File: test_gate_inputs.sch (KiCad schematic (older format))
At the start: 24 parts

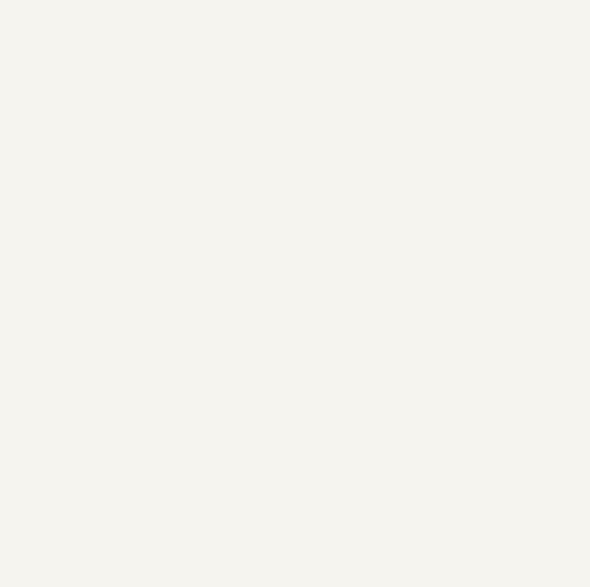
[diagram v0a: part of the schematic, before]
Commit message: add pin header connector
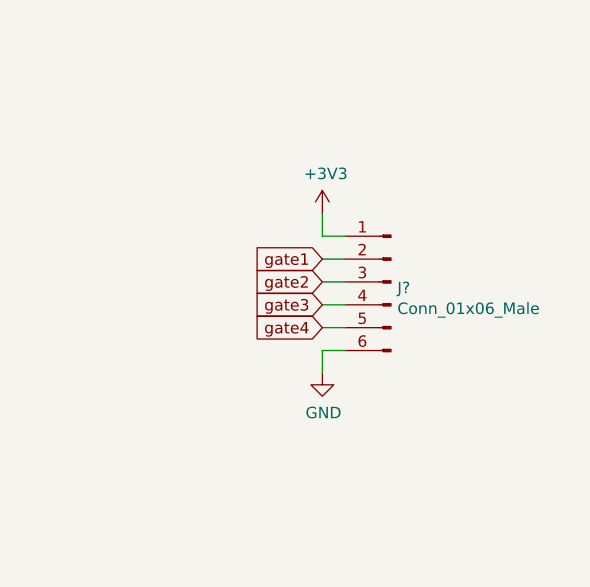
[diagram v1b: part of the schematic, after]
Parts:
- added J?: Conn_01x06_Male, symbol Connector:Conn_01x06_Male
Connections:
- net +3V3: now also J?.1 (Pin_1)
- net GND: now also J?.6 (Pin_6)
- new net gate1: J?.2 (Pin_2)
- new net gate2: J?.3 (Pin_3)
- new net gate3: J?.4 (Pin_4)
- new net gate4: J?.5 (Pin_5)
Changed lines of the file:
@@
 Wire Wire Line
 	3300 6500 3300 6700
+$Comp
+L Connector:Conn_01x06_Male J?
+U 1 1 6128B18E
+P 6500 3350
+F 0 "J?" H 6472 3324 50  0000 R CNN
+F 1 "Conn_01x06_Male" H 6472 3233 50  0000 R CNN
+F 2 "" H 6500 3350 50  0001 C CNN
+F 3 "~" H 6500 3350 50  0001 C CNN
+	1    6500 3350
+	-1   0    0    -1
+$EndComp
+$Comp
+L power:+3V3 #PWR?
+U 1 1 61293AED
+P 6200 3050
+F 0 "#PWR?" H 6200 2900 50  0001 C CNN
+F 1 "+3V3" H 6215 3223 50  0000 C CNN
+F 2 "" H 6200 3050 50  0001 C CNN
+F 3 "" H 6200 3050 50  0001 C CNN
+	1    6200 3050
+	1    0    0    -1
+$EndComp
+$Comp
+L power:GND #PWR?
+U 1 1 61294CF9
+P 6200 3750
+F 0 "#PWR?" H 6200 3500 50  0001 C CNN
+F 1 "GND" H 6205 3577 50  0000 C CNN
+F 2 "" H 6200 3750 50  0001 C CNN
+F 3 "" H 6200 3750 50  0001 C CNN
+	1    6200 3750
+	1    0    0    -1
+$EndComp
+Wire Wire Line
+	6200 3750 6200 3650
+Wire Wire Line
+	6200 3650 6300 3650
+Wire Wire Line
+	6300 3150 6200 3150
+Wire Wire Line
+	6200 3150 6200 3050
+Text GLabel 6200 3350 0    50   Input ~ 0
+gate2
+Text GLabel 6200 3250 0    50   Input ~ 0
+gate1
+Text GLabel 6200 3450 0    50   Input ~ 0
+gate3
+Text GLabel 6200 3550 0    50   Input ~ 0
+gate4
+Wire Wire Line
+	6200 3250 6300 3250
+Wire Wire Line
+	6200 3350 6300 3350
+Wire Wire Line
+	6200 3450 6300 3450
+Wire Wire Line
+	6200 3550 6300 3550
 $EndSCHEMATC

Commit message: connect everything up and annotate
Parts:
- gave numbers to parts that had none: 25
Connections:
- net gate1: now also Q1.3 (C), R9.2
- net gate2: now also Q2.3 (C), R10.2
- net gate3: now also Q3.3 (C), R11.2
- net gate4: now also Q4.3 (C), R12.2

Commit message: fix rules check
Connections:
- net GND: now also J1.TN, J2.TN, J3.TN, J4.TN
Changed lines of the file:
@@
 Wire Wire Line
 	3300 3000 3300 3100
+$Comp
+L power:+3V3 #PWR0123
+U 1 1 612BD10D
+P 7550 1750
+F 0 "#PWR0123" H 7550 1600 50  0001 C CNN
+F 1 "+3V3" H 7565 1923 50  0000 C CNN
+F 2 "" H 7550 1750 50  0001 C CNN
+F 3 "" H 7550 1750 50  0001 C CNN
+	1    7550 1750
+	1    0    0    -1
+$EndComp
+$Comp
+L power:GND #PWR0124
+U 1 1 612BD7F8
+P 8150 1850
+F 0 "#PWR0124" H 8150 1600 50  0001 C CNN
+F 1 "GND" H 8155 1677 50  0000 C CNN
+F 2 "" H 8150 1850 50  0001 C CNN
+F 3 "" H 8150 1850 50  0001 C CNN
+	1    8150 1850
+	1    0    0    -1
+$EndComp
+$Comp
+L power:PWR_FLAG #FLG0101
+U 1 1 612BE96F
+P 7550 1850
+F 0 "#FLG0101" H 7550 1925 50  0001 C CNN
+F 1 "PWR_FLAG" H 7550 2023 50  0000 C CNN
+F 2 "" H 7550 1850 50  0001 C CNN
+F 3 "~" H 7550 1850 50  0001 C CNN
+	1    7550 1850
+	-1   0    0    1
+$EndComp
+Wire Wire Line
+	7550 1750 7550 1850
+Wire Wire Line
+	8150 1750 8150 1850
+$Comp
+L power:PWR_FLAG #FLG0102
+U 1 1 612CB706
+P 8150 1750
+F 0 "#FLG0102" H 8150 1825 50  0001 C CNN
+F 1 "PWR_FLAG" H 8150 1923 50  0000 C CNN
+F 2 "" H 8150 1750 50  0001 C CNN
+F 3 "~" H 8150 1750 50  0001 C CNN
+	1    8150 1750
+	1    0    0    -1
+$EndComp
+Wire Wire Line
+	2050 1400 2150 1400
+Wire Wire Line
+	2150 1400 2150 1600
+Connection ~ 2150 1600
+Wire Wire Line
+	2050 3200 2150 3200
+Wire Wire Line
+	2150 3200 2150 3400
+Connection ~ 2150 3400
+Wire Wire Line
+	2050 5000 2150 5000
+Wire Wire Line
+	2150 5000 2150 5200
+Connection ~ 2150 5200
+Wire Wire Line
+	2050 6800 2150 6800
+Wire Wire Line
+	2150 6800 2150 7000
+Connection ~ 2150 7000
 $EndSCHEMATC
